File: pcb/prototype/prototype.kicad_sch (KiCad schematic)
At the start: 44 parts, among them J1 SDCARD, J2 Bus_ISA_8bit_AB_Rev0, SW1 ADDR SEL, U1 74HC00, U10 74HC74, U11 74HC08, U12 74HC04, U13 74HC74, U2 74HCT32, U3 74HCT139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

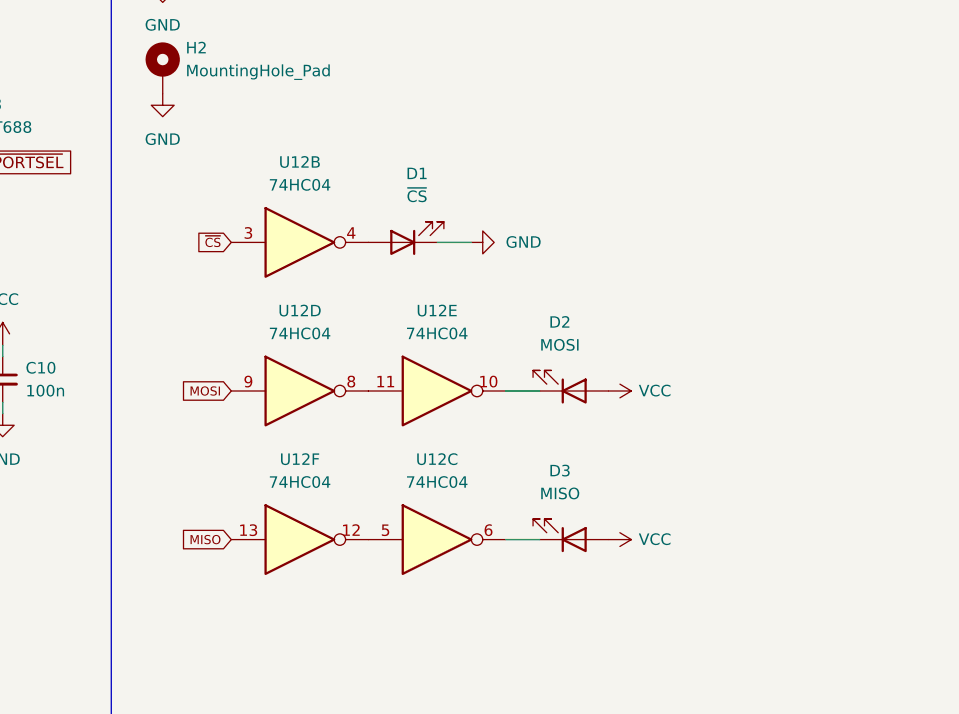
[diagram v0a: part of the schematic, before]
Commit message: Revising prototype, updating software and adding bracket
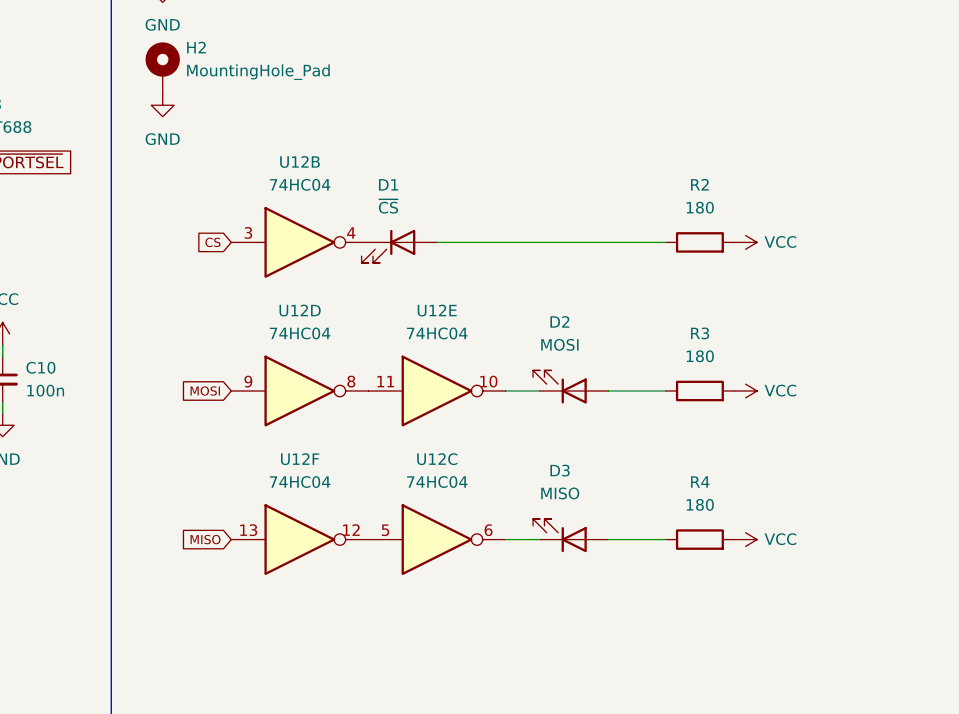
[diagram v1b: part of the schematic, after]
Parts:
- added R2, R3, R4: 180, Resistor_THT:R_Axial_DIN0207_L6.3mm_D2.5mm_P7.62mm_Horizontal, symbol Device:R
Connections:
- net CS: now also U12.3
- net GND: no longer D1.1 (K)
- net VCC: now also R2.2, R3.2, R4.2; no longer D2.2 (A), D3.2 (A)
- net ~{CS}: no longer U12.3
- net at U12.4: now also D1.1 (K); no longer D1.2 (A)
- new net: D1.2 (A), R2.1
- new net: D2.2 (A), R3.1
- new net: D3.2 (A), R4.1
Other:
- moved on the sheet: D1
